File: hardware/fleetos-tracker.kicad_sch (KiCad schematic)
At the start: 1 part, among them U1 STM32L496RGTx

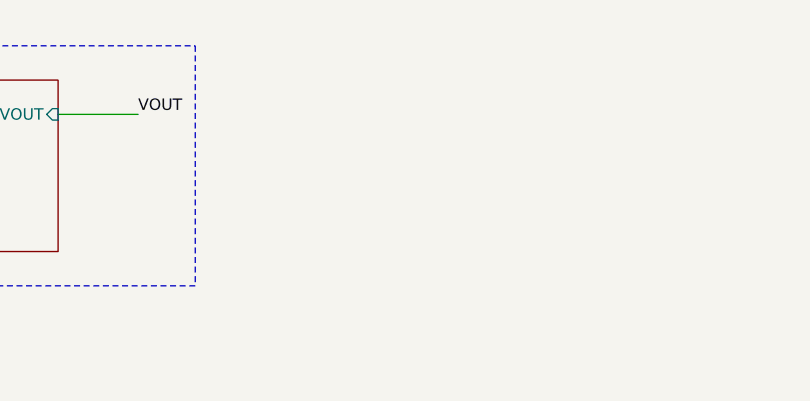
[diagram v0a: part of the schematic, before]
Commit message: implement GNSS receiver
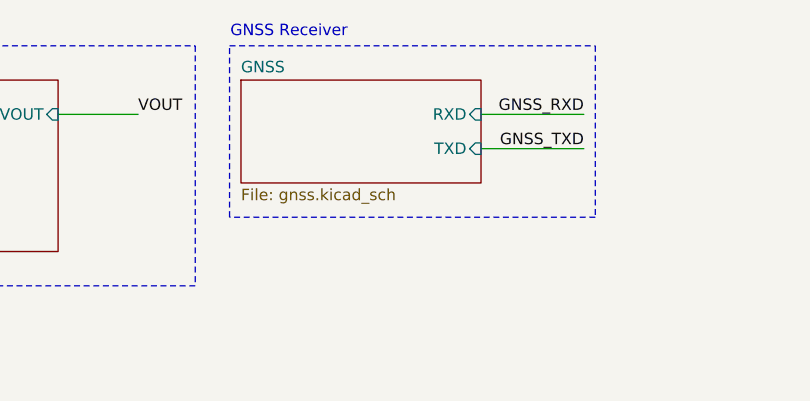
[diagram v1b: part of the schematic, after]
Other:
- added sheet GNSS (gnss.kicad_sch)
- note added: "GNSS Receiver"
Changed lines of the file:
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@@
+		)
+	)
+	(rectangle
+		(start 86.36 16.51)
+		(end 127 35.56)
+		(stroke
+			(width 0)
+			(type dash)
+		)
+		(fill
+			(type none)
 		)
 	)
@@
 		)
 	)
+	(text "GNSS Receiver"
+		(exclude_from_sim no)
+		(at 92.964 14.986 0)
+		(effects
+			(font
+				(size 1.27 1.27)
+			)
+		)
+	)
+	(wire
+		(pts
+			(xy 114.3 24.13) (xy 125.73 24.13)
+		)
+		(stroke
+			(width 0)
+			(type default)
+		)
+	)
 	(wire
 		(pts
@@
 		(pts
 			(xy 16.51 31.75) (xy 27.94 31.75)
+		)
+		(stroke
+			(width 0)
+			(type default)
+		)
+	)
+	(wire
+		(pts
+			(xy 114.3 27.94) (xy 125.73 27.94)
 		)
 		(stroke
@@
 		)
 	)
+	(label "GNSS_RXD"
+		(at 125.73 24.13 180)
+		(effects
+			(font
+				(size 1.27 1.27)
+			)
+			(justify right bottom)
+		)
+	)
 	(label "DVCC"
 		(at 16.51 24.13 0)
@@
 			)
 			(justify left bottom)
+		)
+	)
+	(label "GNSS_TXD"
+		(at 125.73 27.94 180)
+		(effects
+			(font
+				(size 1.27 1.27)
+			)
+			(justify right bottom)
 		)
 	)
@@
 				)
 			)
+		)
+	)
+	(sheet
+		(at 87.63 20.32)
+		(size 26.67 11.43)
+		(exclude_from_sim no)
+		(in_bom yes)
+		(on_board yes)
+		(dnp no)
+		(fields_autoplaced yes)
+		(stroke
+			(width 0.1524)
+			(type solid)
+		)
+		(fill
+			(color 0 0 0 0.0000)
+		)
+		(property "Sheetname" "GNSS"
+			(at 87.63 19.6084 0)
+			(effects
+				(font
+					(size 1.27 1.27)
+				)
+				(justify left bottom)
+			)
+		)
+		(property "Sheetfile" "gnss.kicad_sch"
+			(at 87.63 32.3346 0)
+			(effects
+				(font
+					(size 1.27 1.27)
+				)
+				(justify left top)
+			)
+		)
+		(pin "RXD" input
+			(at 114.3 24.13 0)
+			(effects
+				(font
+					(size 1.27 1.27)
+				)
+				(justify right)
+			)
+		)
+		(pin "TXD" input
+			(at 114.3 27.94 0)
+			(effects
+				(font
+					(size 1.27 1.27)
+				)
+				(justify right)
+			)
+		)
+		(instances
+			(project "fleetos-tracker"
+				(path "/34886a96-89cd-4fc5-ba47-006a1318e849"
+					(page "3")
+				)
+			)

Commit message: implement cell modem
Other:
- added sheet Cellular Modem (cellular_modem.kicad_sch)

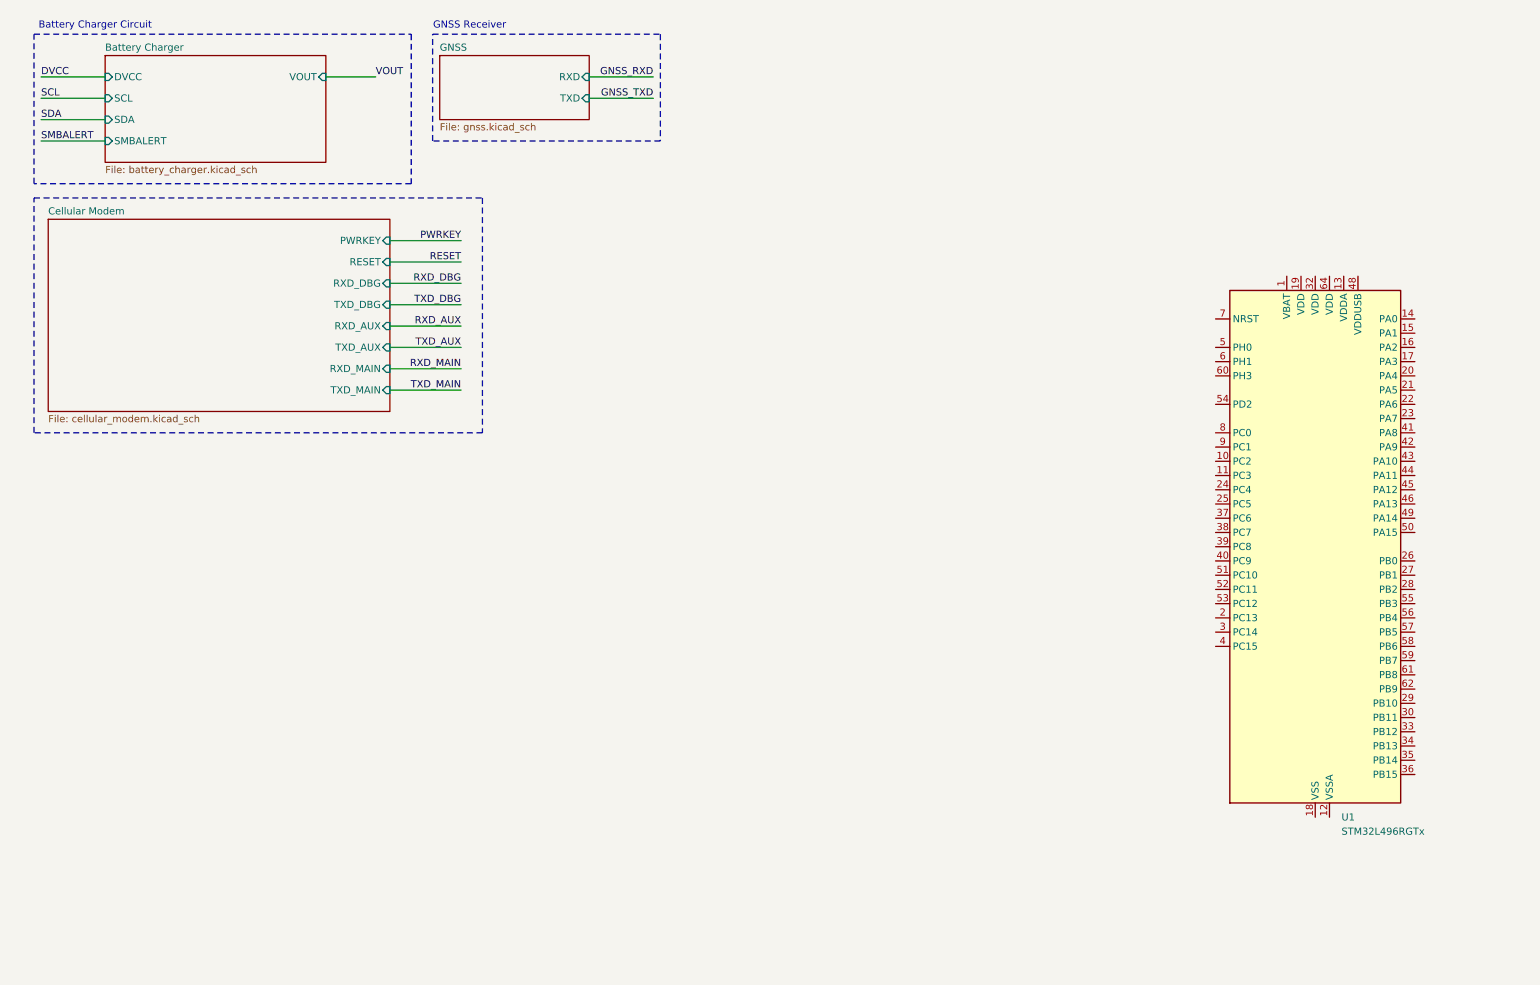
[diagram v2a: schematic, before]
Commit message: begin stm32 implementation and remove battery charger for simplicity
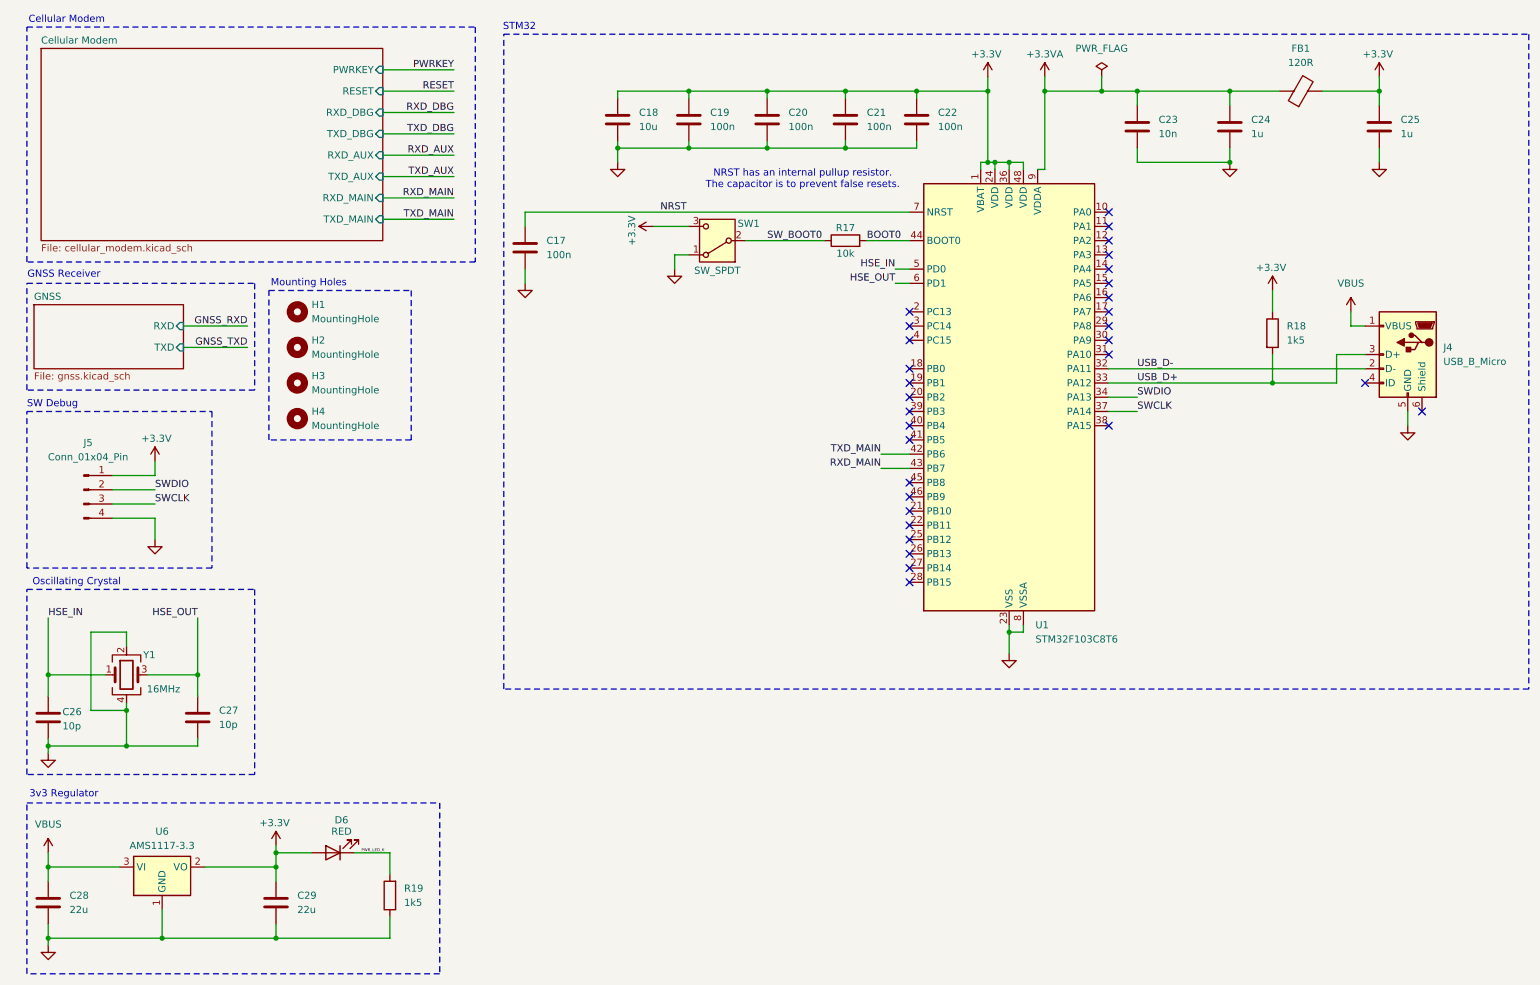
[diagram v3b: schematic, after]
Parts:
- removed U1: STM32L496RGTx, Package_QFP:LQFP-64_10x10mm_P0.5mm, symbol MCU_ST_STM32L4:STM32L496RGTx
- added C17, C19, C20, C21, C22: 100n, Capacitor_SMD:C_0402_1005Metric, symbol Device:C
- added C18: 10u, Capacitor_SMD:C_0603_1608Metric, symbol Device:C
- added C23: 10n, Capacitor_SMD:C_0402_1005Metric, symbol Device:C
- added C24, C25: 1u, Capacitor_SMD:C_0402_1005Metric, symbol Device:C
- added C26, C27: 10p, Capacitor_SMD:C_0402_1005Metric, symbol Device:C
- added C28, C29: 22u, Capacitor_SMD:C_0805_2012Metric, symbol Device:C
- added D6: RED, LED_SMD:LED_0603_1608Metric, symbol Device:LED
- added FB1: 120R, Inductor_SMD:L_0603_1608Metric, symbol Device:FerriteBead
- added H1, H2, H3, H4: MountingHole, MountingHole:MountingHole_2.2mm_M2, symbol Mechanical:MountingHole
- added J4: USB_B_Micro, Connector_USB:USB_Micro-B_Wuerth_629105150521, symbol Connector:USB_B_Micro
- added J5: Conn_01x04_Pin, Connector_PinHeader_2.54mm:PinHeader_1x04_P2.54mm_Vertical, symbol Connector:Conn_01x04_Pin
- added R17: 10k, Resistor_SMD:R_0402_1005Metric, symbol Device:R
- added R18, R19: 1k5, Resistor_SMD:R_0402_1005Metric, symbol Device:R
- added SW1: SW_SPDT, Button_Switch_SMD:SW_SPDT_PCM12, symbol Switch:SW_SPDT
- added U1: STM32F103C8T6, Package_QFP:LQFP-48_7x7mm_P0.5mm, symbol MCU_ST_STM32F1:STM32F103C8Tx
- added U6: AMS1117-3.3, Package_TO_SOT_SMD:SOT-223-3_TabPin2, symbol Regulator_Linear:AMS1117-3.3
- added Y1: 16MHz, Crystal:Crystal_SMD_3225-4Pin_3.2x2.5mm, symbol Device:Crystal_GND24
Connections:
- net RXD_MAIN: now also U1.43 (PB7)
- net TXD_MAIN: now also U1.42 (PB6)
- new net +3.3V: C18.1, C19.1, C20.1, C21.1, C22.1, C25.1, C29.1, D6.2 (A), FB1.2, J5.1 (Pin_1), R18.1, SW1.3 (C), U1.1 (VBAT), U1.24 (VDD), U1.36 (VDD), U1.48 (VDD), U6.2 (VO)
- new net +3.3VA: C23.1, C24.1, FB1.1, U1.9 (VDDA)
- new net BOOT0: R17.2, U1.44 (BOOT0)
- new net GND: C17.2, C18.2, C19.2, C20.2, C21.2, C22.2, C23.2, C24.2, C25.2, C26.2, C27.2, C28.2, C29.2, J4.5 (GND), J5.4 (Pin_4), R19.1, SW1.1 (A), U1.23 (VSS), U1.35 (VSS), U1.47 (VSS), U1.8 (VSSA), U6.1 (GND), Y1.2, Y1.4
- new net HSE_IN: C26.1, U1.5 (PD0), Y1.1
- new net HSE_OUT: C27.1, U1.6 (PD1), Y1.3
- new net NRST: C17.1, U1.7 (NRST)
- new net PWR_LED_K: D6.1 (K), R19.2
- new net SWCLK: J5.3 (Pin_3), U1.37 (PA14)
- new net SWDIO: J5.2 (Pin_2), U1.34 (PA13)
- new net SW_BOOT0: R17.1, SW1.2 (B)
- new net USB_D+: J4.3 (D+), R18.2, U1.33 (PA12)
- new net USB_D-: J4.2 (D-), U1.32 (PA11)
- new net VBUS: C28.1, J4.1 (VBUS), U6.3 (VI)
- no-connect marks 0 -> 31
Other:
- removed sheet Battery Charger
- note added: "3v3 Regulator"
- note added: "Cellular Modem"
- note added: "Mounting Holes"
- note added: "NRST has an internal pullup resistor. The capacitor is to prevent false resets."
- note added: "Oscillating Crystal"
- note added: "STM32"
- note added: "SW Debug"
- note removed: "Battery Charger Circuit"

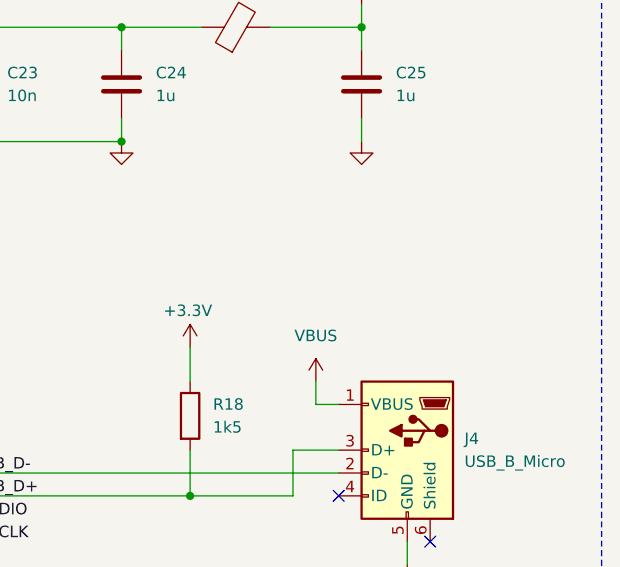
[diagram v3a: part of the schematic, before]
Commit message: refactor power delivery to support higher current loads
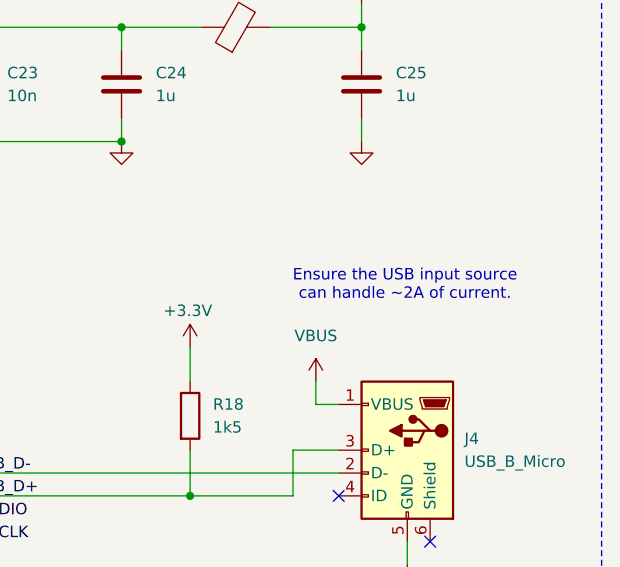
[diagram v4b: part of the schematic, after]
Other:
- note added: "Ensure the USB input source can handle ~2A of current."
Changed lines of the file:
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@@
+		)
+	)
+	(text "Ensure the USB input source \ncan handle ~2A of current."
+		(exclude_from_sim no)
+		(at 260.096 55.372 0)
+		(effects
+			(font
+				(size 1.27 1.27)
+			)
 		)
 	)
